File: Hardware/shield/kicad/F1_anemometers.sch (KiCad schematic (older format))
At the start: 22 parts, among them U1 MCP6244

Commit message: move to digital 1.1.1
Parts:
- removed R35: 100, Discret:R3-LARGE_PADS, symbol R
- removed U1: MCP6244, Housings_DIP:DIP-14_W7.62mm_LongPads, symbol MCP6004
- added U201: LMV358, Housings_DIP:DIP-8_W7.62mm_LongPads, symbol LM358-RESCUE-Windlogger
- D201: renamed from D1; footprint Discret:DO-35 -> Diodes_ThroughHole:Diode_DO-35_SOD27_Horizontal_RM10
- D202: renamed from D2; footprint Discret:DO-35 -> Diodes_ThroughHole:Diode_DO-35_SOD27_Horizontal_RM10
- D203: renamed from D3; footprint Discret:DO-35 -> Diodes_ThroughHole:Diode_DO-35_SOD27_Horizontal_RM10
- D204: renamed from D4; footprint Discret:DO-35 -> Diodes_ThroughHole:Diode_DO-35_SOD27_Horizontal_RM10
- R201: renamed from R2; footprint Discret:R3-LARGE_PADS -> Discret:R4
- R202: renamed from R6; footprint Discret:R3-LARGE_PADS -> Discret:R4
- R203: renamed from R8; footprint Discret:R3-LARGE_PADS -> Discret:R4
- R204: renamed from R4; footprint Discret:R3-LARGE_PADS -> Discret:R4
- R205: renamed from R9; footprint Discret:R3-LARGE_PADS -> Discret:R4
- R206: renamed from R5; footprint Discret:R3-LARGE_PADS -> Discret:R4
- R207: renamed from R10; footprint Discret:R3-LARGE_PADS -> Discret:R4
- R208: renamed from R3; footprint Discret:R3-LARGE_PADS -> Discret:R4
- R209: renamed from R7; footprint Discret:R3-LARGE_PADS -> Discret:R4
- renumbered C3 to C201, C5 to C202, C4 to C203, JP1 to JP201, JP3 to JP202, JP2 to JP203, JP4 to JP204
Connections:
- net +5V: now also U201.8 (V+), U201.8 (V+)
- net GND: now also U201.4 (V-), U201.4 (V-)
- net Speed1: now also U201.1
- net Speed2: now also U201.7
- net at R206.1, R208.1: now also U201.3 (+)
- net at R207.1, R209.1: now also U201.5 (+)
- net at JP201.3: now also JP203.3, R204.2
- net at D201.2 (A), D202.1 (K), JP203.2: now also U201.2 (-)
- net at D203.2 (A), D204.1 (K), JP204.2: now also U201.6 (-)
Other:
- note added: "??"
- moved on the sheet: R206, R207, R208, R209

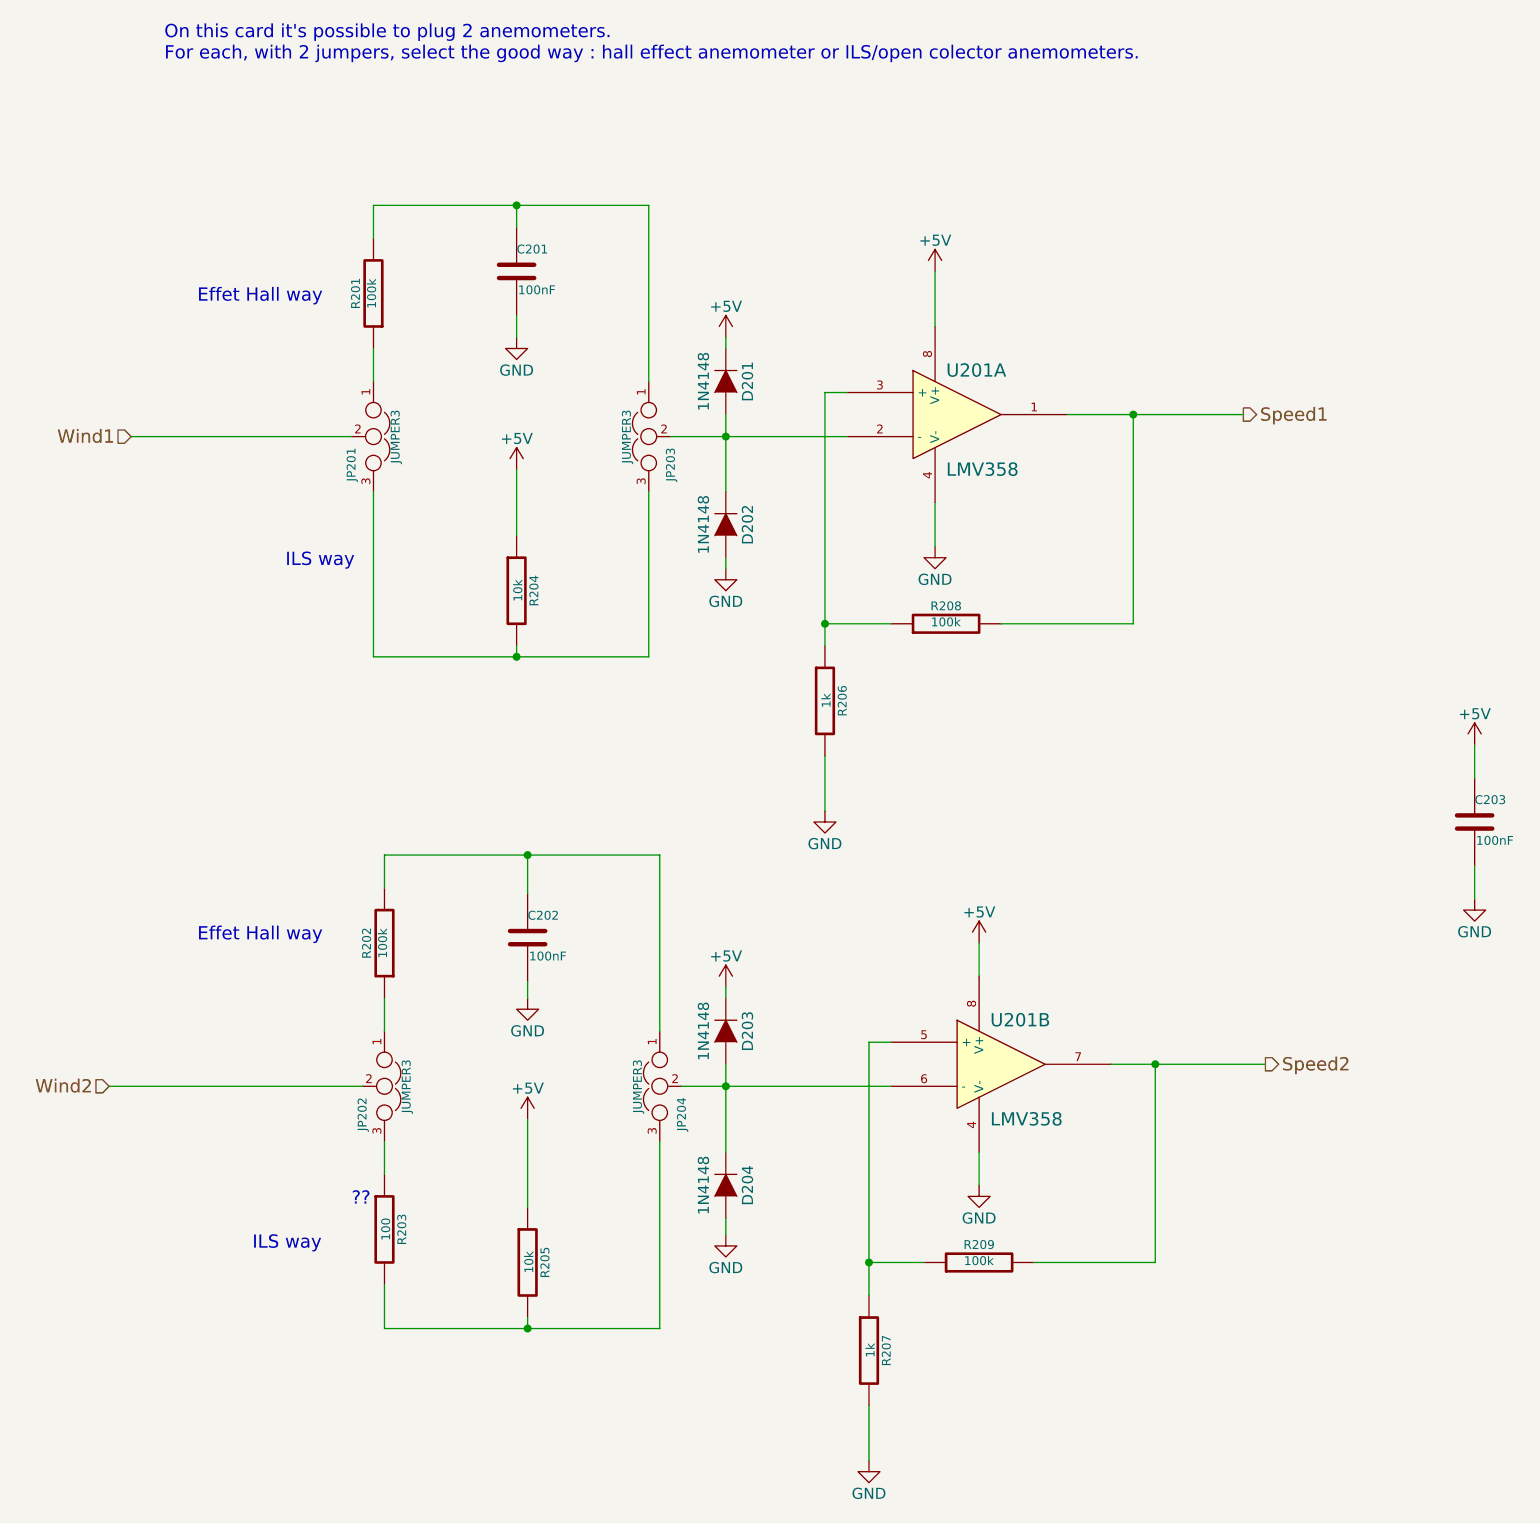
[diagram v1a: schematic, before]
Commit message: Update shield to 2.0.0
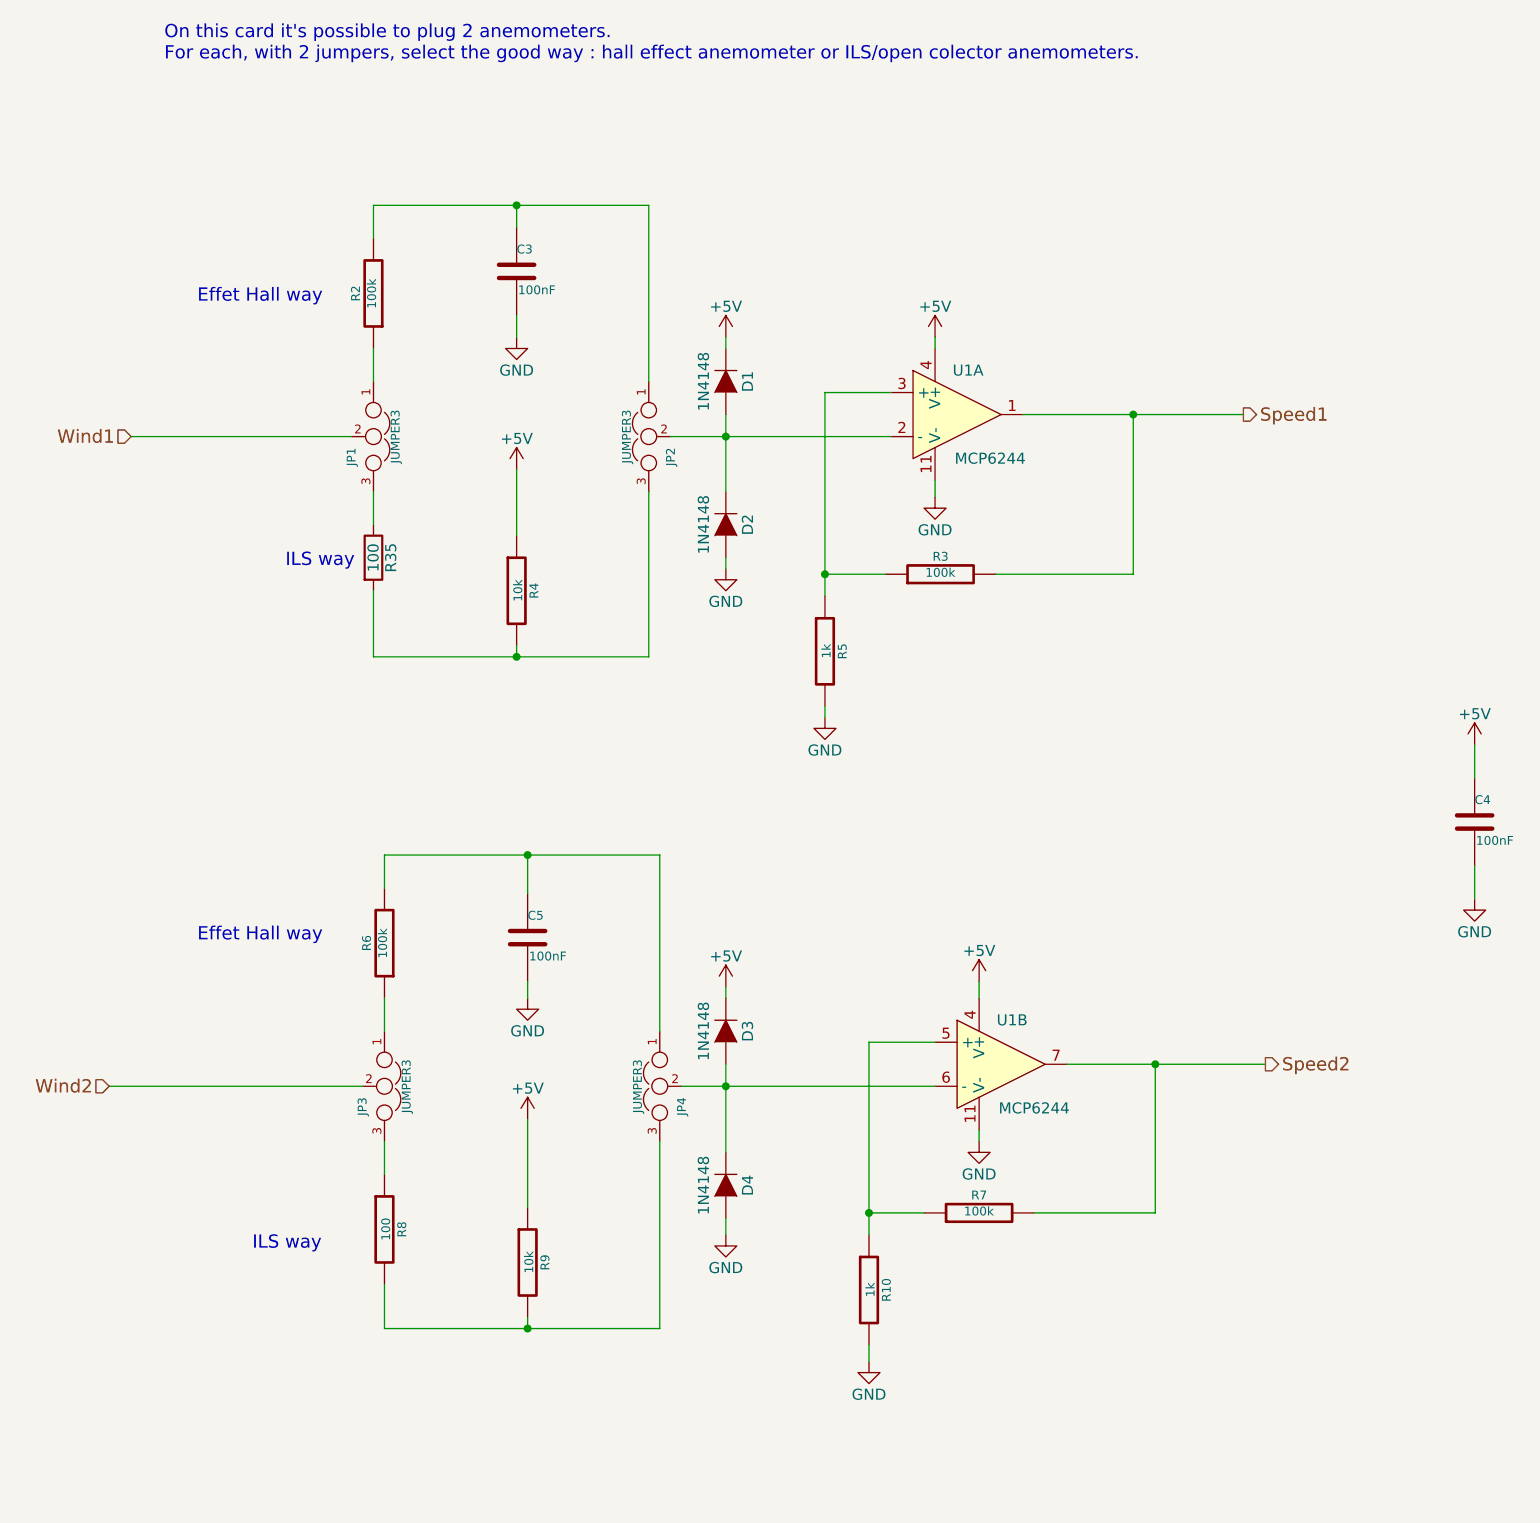
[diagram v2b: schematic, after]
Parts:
- removed U201: LMV358, Housings_DIP:DIP-8_W7.62mm_LongPads, symbol LM358-RESCUE-Windlogger
- added R35: 100, Discret:R3-LARGE_PADS, symbol R
- added U1: MCP6244, Housings_DIP:DIP-14_W7.62mm_LongPads, symbol MCP6004
- D1: renamed from D201; footprint Diodes_ThroughHole:Diode_DO-35_SOD27_Horizontal_RM10 -> Discret:DO-35
- D2: renamed from D202; footprint Diodes_ThroughHole:Diode_DO-35_SOD27_Horizontal_RM10 -> Discret:DO-35
- D3: renamed from D203; footprint Diodes_ThroughHole:Diode_DO-35_SOD27_Horizontal_RM10 -> Discret:DO-35
- D4: renamed from D204; footprint Diodes_ThroughHole:Diode_DO-35_SOD27_Horizontal_RM10 -> Discret:DO-35
- R10: renamed from R207; footprint Discret:R4 -> Discret:R3-LARGE_PADS
- R2: renamed from R201; footprint Discret:R4 -> Discret:R3-LARGE_PADS
- R3: renamed from R208; footprint Discret:R4 -> Discret:R3-LARGE_PADS
- R4: renamed from R204; footprint Discret:R4 -> Discret:R3-LARGE_PADS
- R5: renamed from R206; footprint Discret:R4 -> Discret:R3-LARGE_PADS
- R6: renamed from R202; footprint Discret:R4 -> Discret:R3-LARGE_PADS
- R7: renamed from R209; footprint Discret:R4 -> Discret:R3-LARGE_PADS
- R8: renamed from R203; footprint Discret:R4 -> Discret:R3-LARGE_PADS
- R9: renamed from R205; footprint Discret:R4 -> Discret:R3-LARGE_PADS
- renumbered C201 to C3, C203 to C4, C202 to C5, JP201 to JP1, JP203 to JP2, JP202 to JP3, JP204 to JP4
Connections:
- net +5V: now also U1.4 (V+), U1.4 (V+)
- net GND: now also U1.11 (V-), U1.11 (V-)
- net Speed1: now also U1.1
- net Speed2: now also U1.7
- net at D1.2 (A), D2.1 (K), JP2.2: now also U1.2 (-)
- net at R3.1, R5.1: now also U1.3 (+)
- net at R10.1, R7.1: now also U1.5 (+)
- net at D3.2 (A), D4.1 (K), JP4.2: now also U1.6 (-)
- net at JP2.3, R4.2: now also R35.2; no longer JP1.3
- new net: JP1.3, R35.1
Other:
- note removed: "??"
- moved on the sheet: R10, R3, R5, R7
